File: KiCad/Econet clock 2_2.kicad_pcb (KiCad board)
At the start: 2 copper layers, 56.3 x 45.5 mm, 21 parts, among them IC1 ATtiny45-20PU, J1 Conn_01x02_Male, J2 Conn_01x02_Pin, J3 Conn_01x06_Pin, SW1 SW_DIP_x04

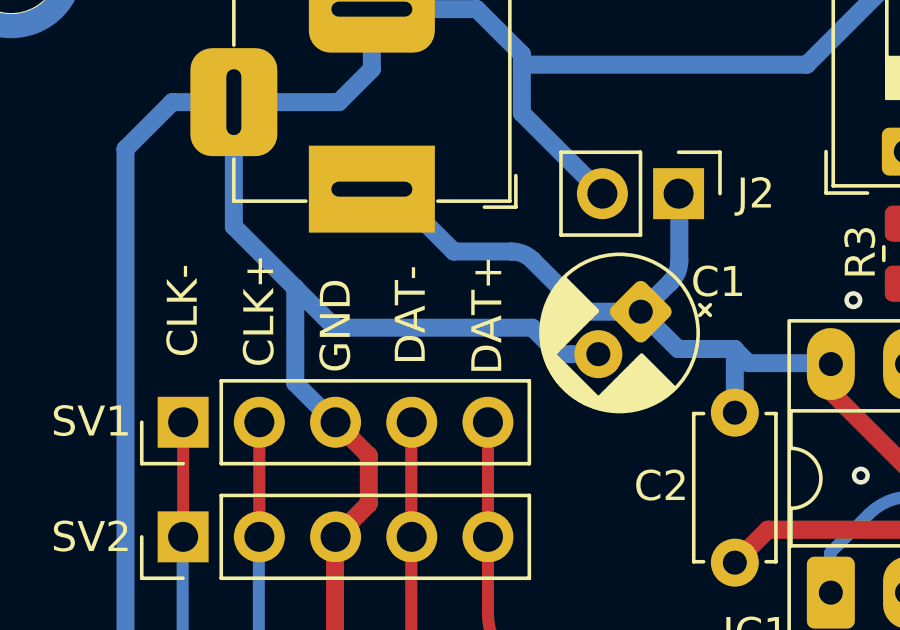
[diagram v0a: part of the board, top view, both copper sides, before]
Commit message: Updated data polarity markings, increased decoupling capacitance
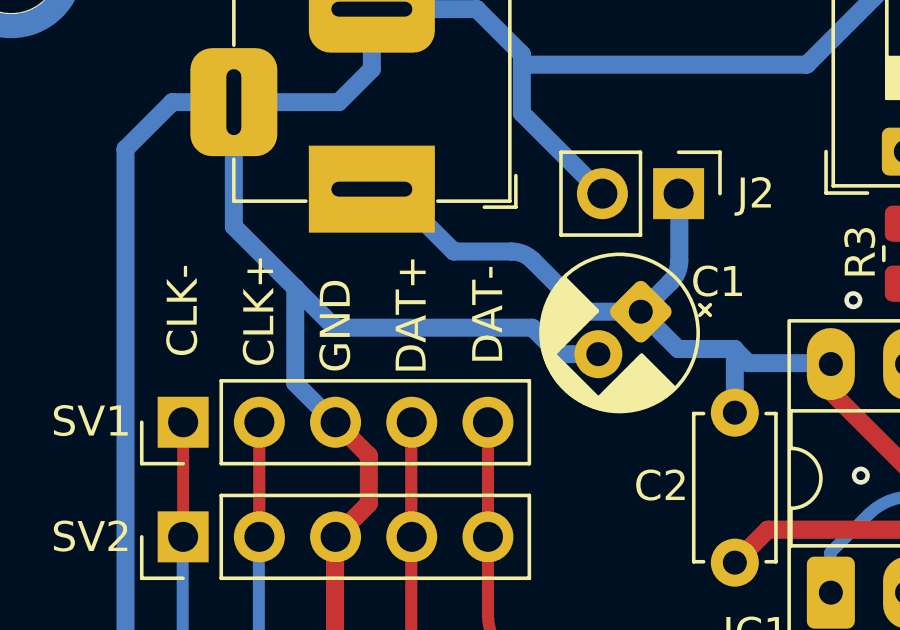
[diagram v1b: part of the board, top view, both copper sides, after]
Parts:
- SV1: value Ext DIN header 1 -> Header 1
- SV2: value Ext DIN Header 2 -> Header 2
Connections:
- SV1 pad 4: /DATA- -> /DATA+
- SV1 pad 5: /DATA+ -> /DATA-
- SV2 pad 4: /DATA- -> /DATA+
- SV2 pad 5: /DATA+ -> /DATA-
- SV3 pad 1: /DATA- -> /DATA+
- SV3 pad 4: /DATA+ -> /DATA-
- SV4 pad 1: /DATA- -> /DATA+
- SV4 pad 4: /DATA+ -> /DATA-
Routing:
- net /DATA-: track 45.3 -> 40.7 mm
- net /DATA+: track 40.7 -> 45.3 mm
